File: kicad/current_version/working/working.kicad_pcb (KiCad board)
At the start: 2 copper layers, 45 x 45 mm, 16 parts, among them J1 scuath, J2 scumcsm, J3 scumcsm, J4 swsi1h, J5 sws2880, U1 imsp10mpump21rs2227

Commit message: workings
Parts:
- SW2: renamed from J4; footprint all_the_kicad_footprints_one_library:kicad_connector_pinheader_2_54mm_pinheader_1x03_p2_54mm_vertical -> oomlout_oomp_part_footprints:swsi1h_electronic_switch_slide_2d54_header_single_pole_double_throw
- renumbered J2 to CON1, J3 to CON2, J1 to CON3, U1 to IC1, J5 to SW1
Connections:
- net /out_1 renamed /select
- net /out_2 renamed /slide_switch_out_2
- CON1 pad 2: /usb_negative_secondary_2 -> /usb_negative_secondary_1
- CON1 pad 3: /usb_positive_secondary_2 -> /usb_positive_secondary_1
- CON1 pad 4: /usb_id -> /usb_id_secondary_1
- CON2 pad 2: /usb_negative_secondary_1 -> /usb_negative_secondary_2
- CON2 pad 3: /usb_positive_secondary_1 -> /usb_positive_secondary_2
- CON2 pad 4: /usb_id -> /usb_id_secondary_2

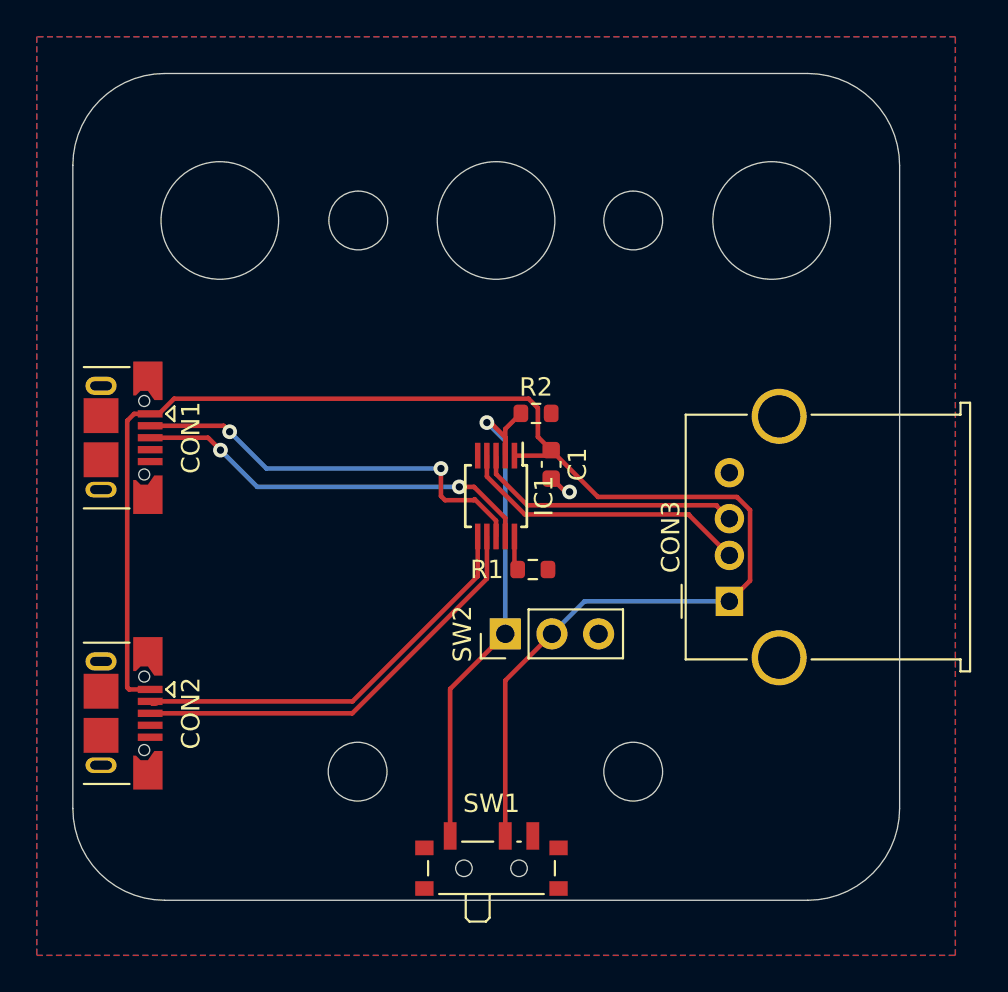
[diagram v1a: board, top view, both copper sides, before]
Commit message: added power mux
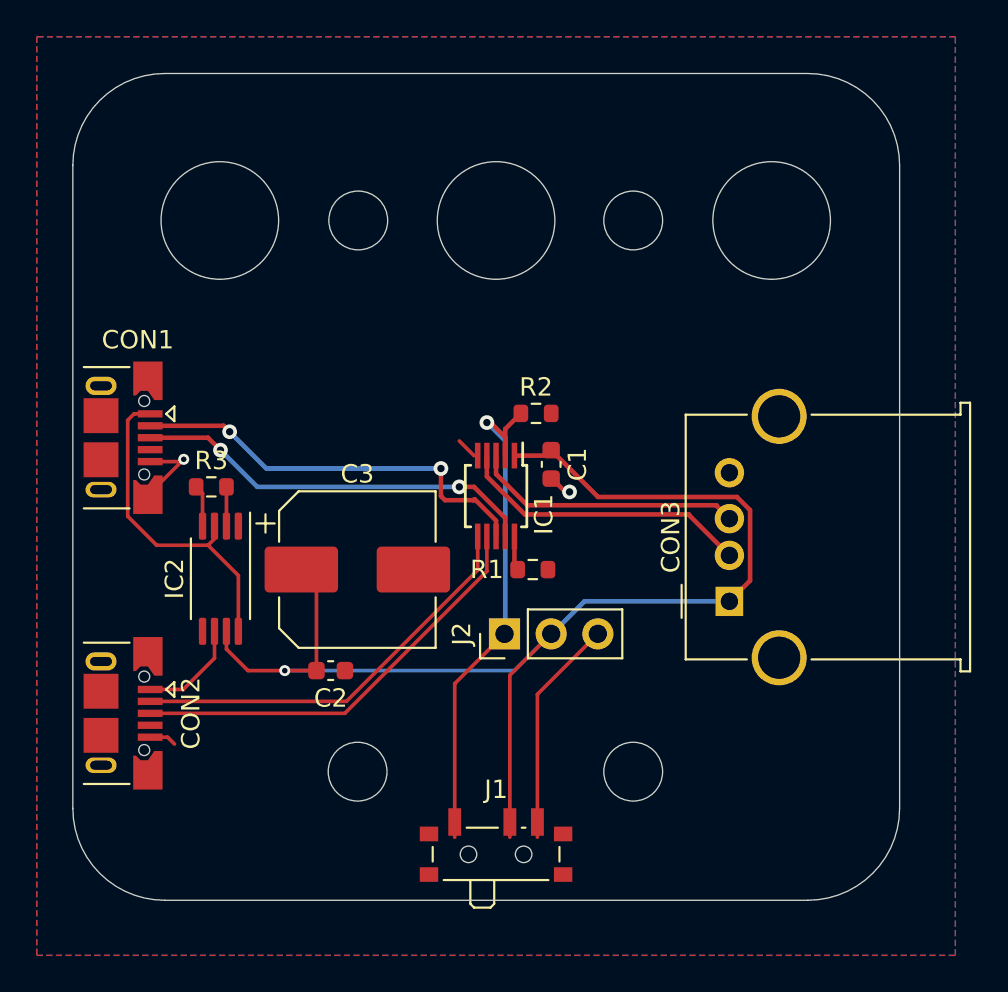
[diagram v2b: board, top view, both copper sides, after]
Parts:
- removed SW1: sws2880, oomlout_oomp_part_footprints:sws2880_electronic_switch_slide_2_8_mm_x_8_mm_x_1_4_single_pole_double_throw
- removed SW2: swsi1h, oomlout_oomp_part_footprints:swsi1h_electronic_switch_slide_2d54_header_single_pole_double_throw
- added C2: c6nf100, oomlout_oomp_part_footprints:c6nf100_electronic_capacitor_0603_100_nano_farad, F.Cu at (-9.00, 9.50)
- added C3: c8d65tuf220v10, oomlout_oomp_part_footprints:c8d65tuf220v10_electronic_capacitor_8_mm_diameter_6_5_mm_tall_electrolytic_220_micro_farad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, F.Cu at (-7.55, 4.00)
- added IC2: itssp8mpptps2113, oomlout_oomp_part_footprints:itssp8mpptps2113_electronic_ic_tssop_8_multiplexer_power_multiplexer_texas_instruments_tps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, F.Cu at (-15.0, 4.50)
- added J1: sws2880s, oomlout_oomp_part_footprints:sws2880s_electronic_switch_slide_2_8_mm_x_8_mm_x_1_4_mm_surface_mount_single_pole_double_t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, F.Cu at (0.00, 19.2)
- added J2: swsi1hs, oomlout_oomp_part_footprints:swsi1hs_electronic_switch_slide_2d54_header_surface_mount_single_pole_double_throw, F.Cu at (0.46, 7.50)
- added R3: r6o271, oomlout_oomp_part_footprints:r6o271_electronic_resistor_0603_270_ohm, F.Cu at (-15.5, -0.50)
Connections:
- CON1 pad 1: +5V -> /5v_in_1_zz
- CON1 pad 2: /usb_negative_secondary_1 -> /usb_negative_secondary_2
- CON1 pad 3: /usb_positive_secondary_1 -> /usb_positive_secondary_2
- CON1 pad 4: /usb_id_secondary_1 -> /usb_id_secondary_2
- CON2 pad 1: +5V -> /5v_in_2_zz
- CON2 pad 2: /usb_negative_secondary_2 -> /usb_negative_secondary_1
- CON2 pad 3: /usb_positive_secondary_2 -> /usb_positive_secondary_1
- CON2 pad 4: /usb_id_secondary_2 -> /usb_id_secondary_1
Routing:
- net /5v_in_1_zz: track 0.00 -> 18.2 mm
- net +5V: track 83.6 -> 69.6 mm, vias 0 -> 1
- net /slide_switch_out_2: track 0.00 -> 12.4 mm
- net GND: track 1.62 -> 11.0 mm, vias 1 -> 2
- net /5v_in_2_zz: track 0.00 -> 5.67 mm
- net Net-(IC2-___ilim): track 0.00 -> 2.28 mm
- net /usb_negative_secondary_1: track 23.2 -> 22.6 mm

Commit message: production update
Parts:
- removed J2: swsi1hs, oomlout_oomp_part_footprints:swsi1hs_electronic_switch_slide_2d54_header_surface_mount_single_pole_double_throw
- added J3: hi14pth, oomlout_oomp_part_footprints:hi14pth_electronic_header_2_54_mm_4_pin_through_hole, F.Cu at (-15.5, -6.00)
- added J4: hi14pth, oomlout_oomp_part_footprints:hi14pth_electronic_header_2_54_mm_4_pin_through_hole, F.Cu at (-12.5, 18.5)
- added SW1: sws2880s, oomlout_oomp_part_footprints:sws2880s_electronic_switch_slide_2_8_mm_x_8_mm_x_1_4_mm_surface_mount_single_pole_double_t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, F.Cu at (0.00, 19.5)
- added SW2: swsi1hs, oomlout_oomp_part_footprints:swsi1hs_electronic_switch_slide_2_54_header_surface_mount_single_pole_double_throw, F.Cu at (-0.04, 7.50)
- J1: value sws2880s -> hi14pth; footprint oomlout_oomp_part_footprints:sws2880s_electronic_switch_slide_2_8_mm_x_8_mm_x_1_4_mm_surface_mount_single_pole_double_t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 -> oomlout_oomp_part_footprints:hi14pth_electronic_header_2_54_mm_4_pin_through_hole
- moved J1 23.1 mm to (19.0, 6.00), turned to 180 degrees
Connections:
- J1 pad 1: /select -> +5V
- J1 pad 2: +5V -> /usb_negative_main
- J1 pad 3: /slide_switch_out_2 -> /usb_positive_main
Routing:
- net /5v_in_2_zz: track 5.67 -> 17.3 mm, vias 0 -> 1
- net /usb_positive_secondary_1: track 23.4 -> 31.3 mm, vias 0 -> 1
- net /usb_negative_secondary_1: track 22.6 -> 30.3 mm, vias 0 -> 1
- net /usb_positive_secondary_2: track 22.1 -> 29.5 mm
- net GND: track 11.0 -> 17.4 mm
- net /usb_positive_main: track 14.7 -> 21.2 mm
- net +5V: track 69.6 -> 76.1 mm
- net /usb_negative_main: track 16.1 -> 22.5 mm
- net /5v_in_1_zz: track 18.2 -> 23.5 mm, vias 0 -> 1
- net /usb_negative_secondary_2: track 22.8 -> 27.8 mm, vias 2 -> 3
